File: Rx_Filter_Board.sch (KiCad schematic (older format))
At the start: 100 parts, among them K1 HK4100, K10 HK4100, K11 HK4100, K12 HK4100, K13 HK4100, K2 HK4100, K3 HK4100, K4 HK4100, K5 HK4100, K6 HK4100, K7 HK4100, K8 HK4100, K9 HK4100, P1 BNC, P2 BNC, P3 BNC, P4 CONN_01X08, P6 CONN_01X02, U1 ULN2003

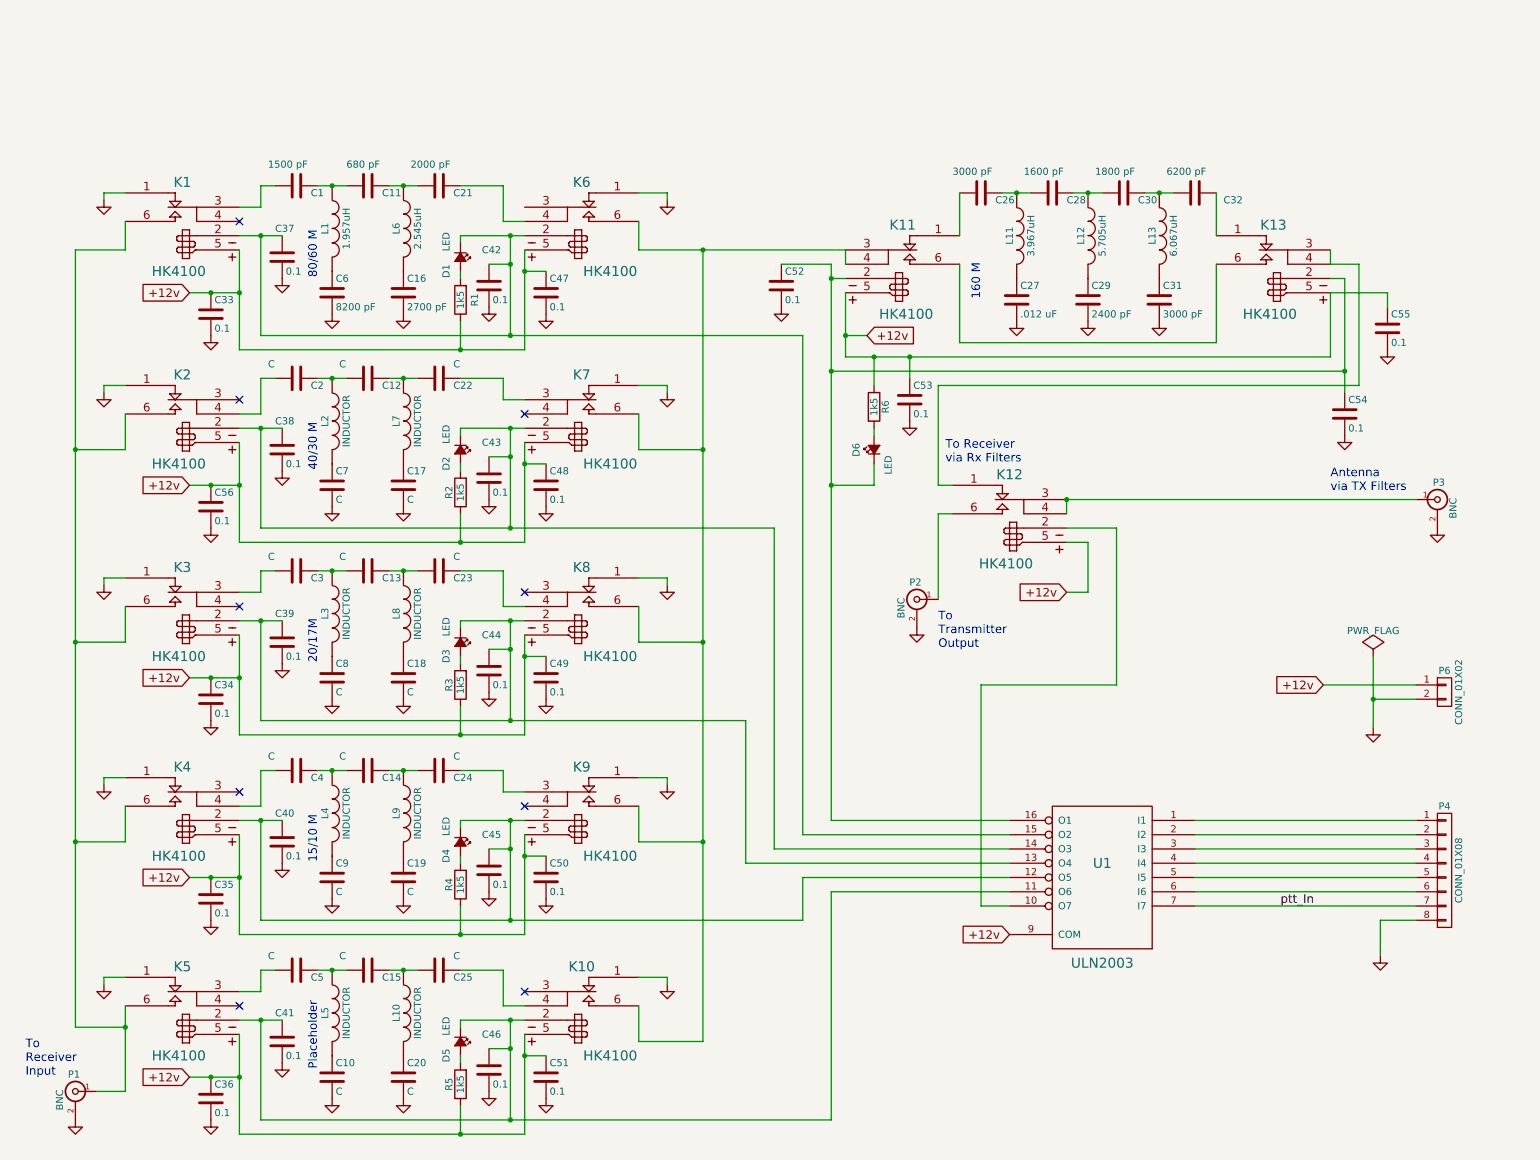
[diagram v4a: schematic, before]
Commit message: Final fabrication with LCD serial driver added
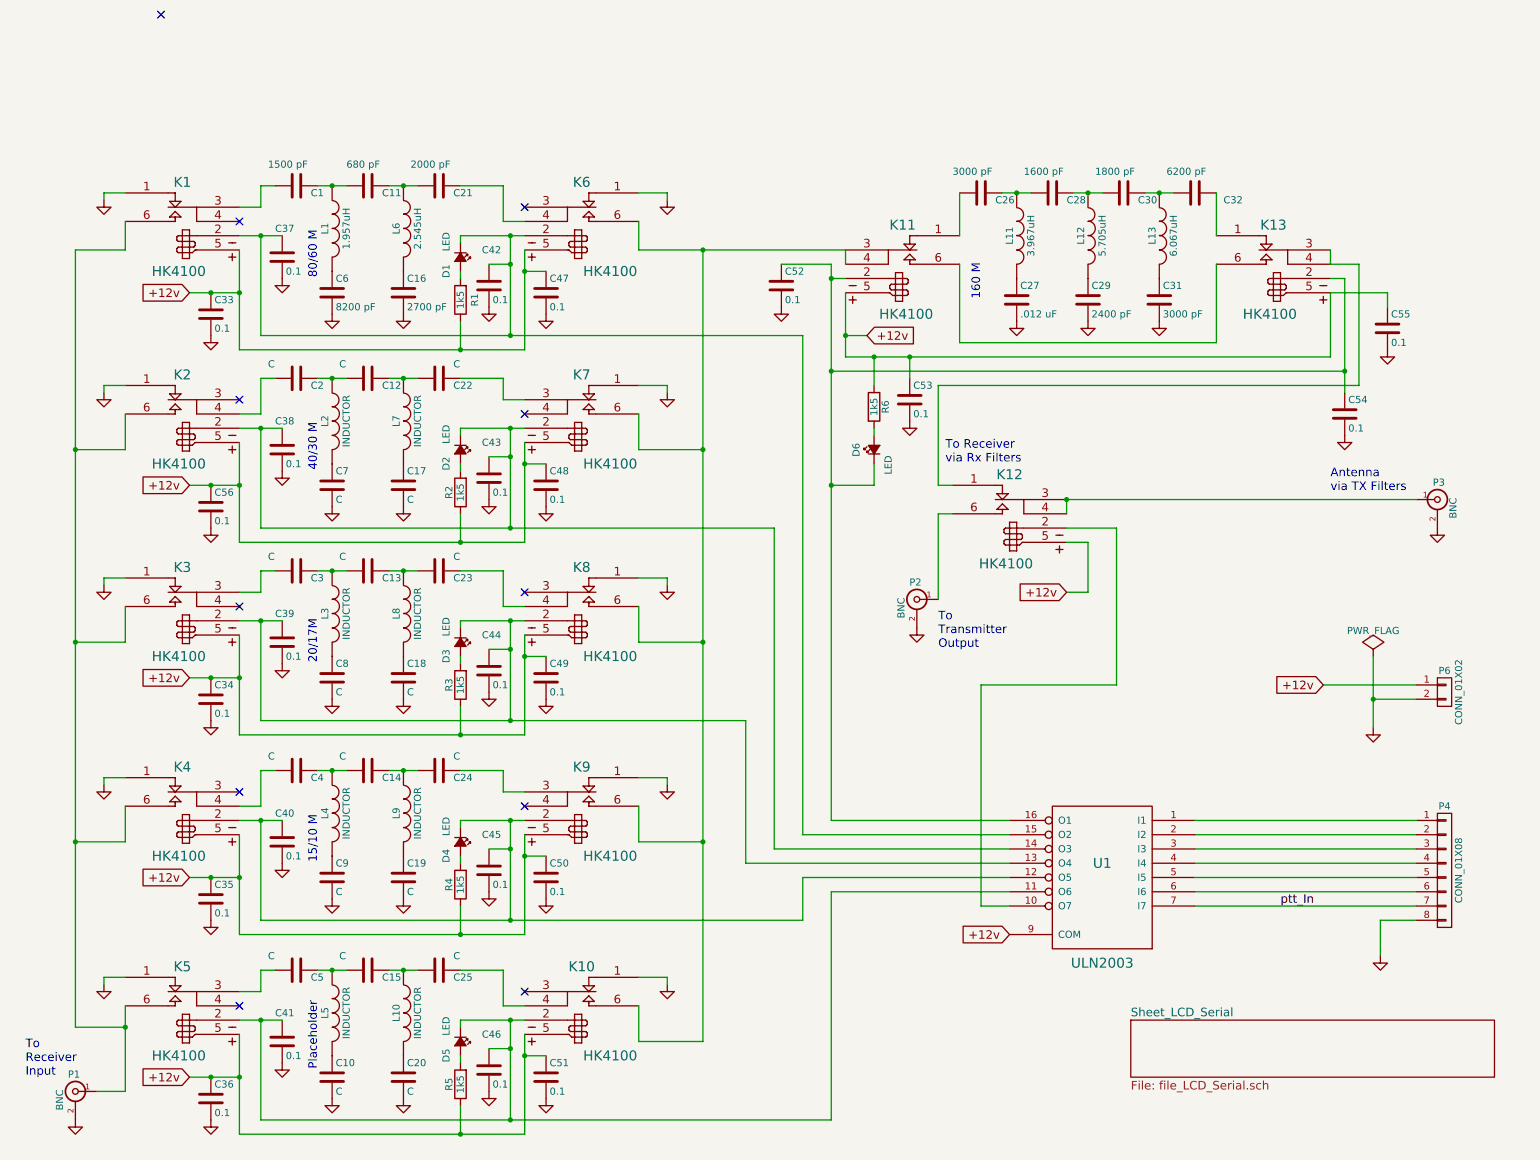
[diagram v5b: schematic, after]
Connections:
- no-connect marks 9 -> 11
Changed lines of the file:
@@
 EESchema Schematic File Version 2
+LIBS:Rx_Filter_Board-rescue
 LIBS:power
 LIBS:device
@@
 LIBS:valves
 LIBS:relays_G
-LIBS:Rx_Filter_Board-rescue
+LIBS:74xx_gj
 LIBS:Rx_Filter_Board-cache
 EELAYER 25 0
@@
 $Descr A4 11693 8268
 encoding utf-8
-Sheet 1 1
+Sheet 1 2
 Title "Receive Filter Board"
 Date "17 oct 2013"
@@
 	2350 2600 2350 3300
 Wire Wire Line
-	4350 3300 2350 3300
-Wire Wire Line
-	4350 2600 4350 3300
+	2350 3300 4350 3300
+Wire Wire Line
+	4350 3300 4350 2600
 Wire Wire Line
 	2000 2900 2350 2900
@@
 	2350 3950 2350 4650
 Wire Wire Line
-	4350 4650 2350 4650
-Wire Wire Line
-	4350 3950 4350 4650
+	2350 4650 4350 4650
+Wire Wire Line
+	4350 4650 4350 3950
 Wire Wire Line
 	2000 4250 2350 4250
@@
 	2350 5350 2350 6050
 Wire Wire Line
-	4350 6050 2350 6050
-Wire Wire Line
-	4350 5350 4350 6050
+	2350 6050 4350 6050
+Wire Wire Line
+	4350 6050 4350 5350
 Wire Wire Line
 	2000 5650 2350 5650
@@
 	2350 1250 2350 1950
 Wire Wire Line
-	4350 1950 2350 1950
-Wire Wire Line
-	4350 1250 4350 1950
+	2350 1950 4350 1950
+Wire Wire Line
+	4350 1950 4350 1250
 Wire Wire Line
 	2000 1550 2350 1550
@@
 	2350 6750 2350 7450
 Wire Wire Line
-	4350 7450 2350 7450
-Wire Wire Line
-	4350 6750 4350 7450
+	2350 7450 4350 7450
+Wire Wire Line
+	4350 7450 4350 6750
 Wire Wire Line
 	2000 7050 2350 7050
@@
 NoConn ~ 2350 2300
 NoConn ~ 2350 1050
+$Sheet
+S 8600 6650 2550 400
+U 57FC0F36
+F0 "Sheet_LCD_Serial" 60
+F1 "file_LCD_Serial.sch" 60
+$EndSheet
+NoConn ~ 4350 950
+NoConn ~ 1800 -400
 $EndSCHEMATC
